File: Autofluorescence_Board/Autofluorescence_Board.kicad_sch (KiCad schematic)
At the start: 0 parts

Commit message: I have no idea
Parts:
- added U1: PAM2863ECR, SOIC_863ECR_DIO, symbol AF_SymbolLibrary:PAM2863ECR
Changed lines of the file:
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@@
 	(generator_version "10.0")
 	(paper "A4")
+	(symbol
+		(lib_id "AF_SymbolLibrary:PAM2863ECR")
+		(at 58.42 60.96 0)
+		(unit 1)
+		(body_style 1)
+		(exclude_from_sim no)
+		(in_bom yes)
+		(on_board yes)
+		(in_pos_files yes)
+		(dnp no)
+		(fields_autoplaced yes)
+		(property "Reference" "U1"
+			(at 81.28 50.8 0)
+			(show_name no)
+			(do_not_autoplace no)
+			(effects
+				(font
+					(size 1.524 1.524)
+				)
+			)
+		)
+		(property "Value" "PAM2863ECR"
+			(at 81.28 53.34 0)
+			(show_name no)
+			(do_not_autoplace no)
+			(effects
+				(font
+					(size 1.524 1.524)
+				)
+			)
+		)
+		(property "Footprint" "SOIC_863ECR_DIO"
+			(at 58.42 60.96 0)
+			(hide yes)
+			(show_name no)
+			(do_not_autoplace no)
+			(effects
+				(font
+					(size 1.27 1.27)
+					(italic yes)
+				)
+			)
+		)
+		(property "Datasheet" "PAM2863ECR"
+			(at 58.42 60.96 0)
+			(hide yes)
+			(show_name no)
+			(do_not_autoplace no)
+			(effects
+				(font
+					(size 1.27 1.27)
+					(italic yes)
+				)
+			)
+		)
+		(property "Description" ""
+			(at 58.42 60.96 0)
+			(hide yes)
+			(show_name no)
+			(do_not_autoplace no)
+			(effects
+				(font
+					(size 1.27 1.27)
+				)
+			)
+		)
+		(pin "1"
+		)
+		(pin "2"
+		)
+		(pin "5"
+		)
+		(pin "6"
+		)
+		(pin "4"
+		)
+		(pin "3"
+		)
+		(pin "8"
+		)
+		(pin "7"
+		)
+		(pin "EPAD"
+		)
+		(instances
+			(project "Autofluorescence_Board"
+				(path "/72deb9c7-3e3f-41e9-884c-65f2f5e1cc20"
+					(reference "U1")
+					(unit 1)
+				)
+			)
+		)
+	)
 	(sheet_instances
 		(path "/"

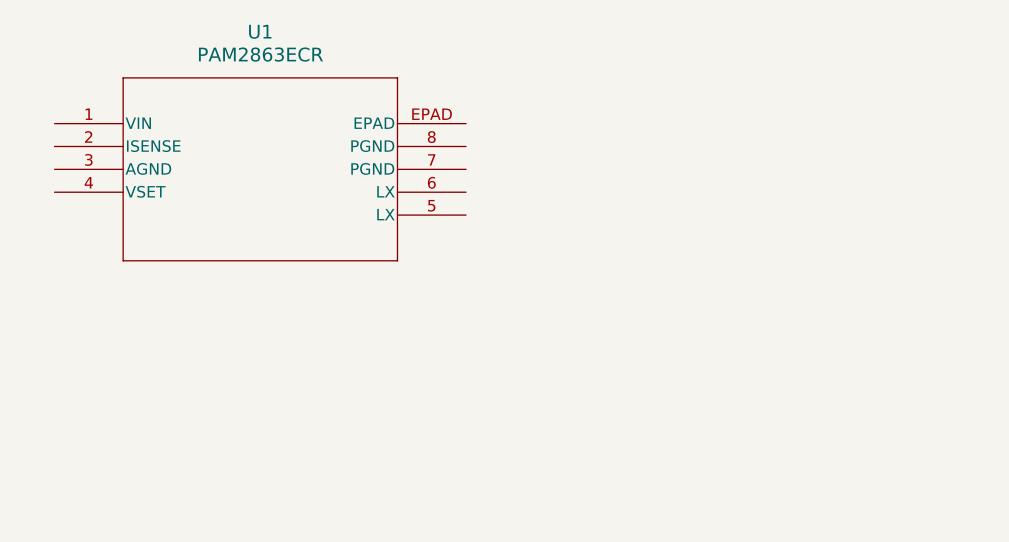
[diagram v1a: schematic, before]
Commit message: Added components to Schematic
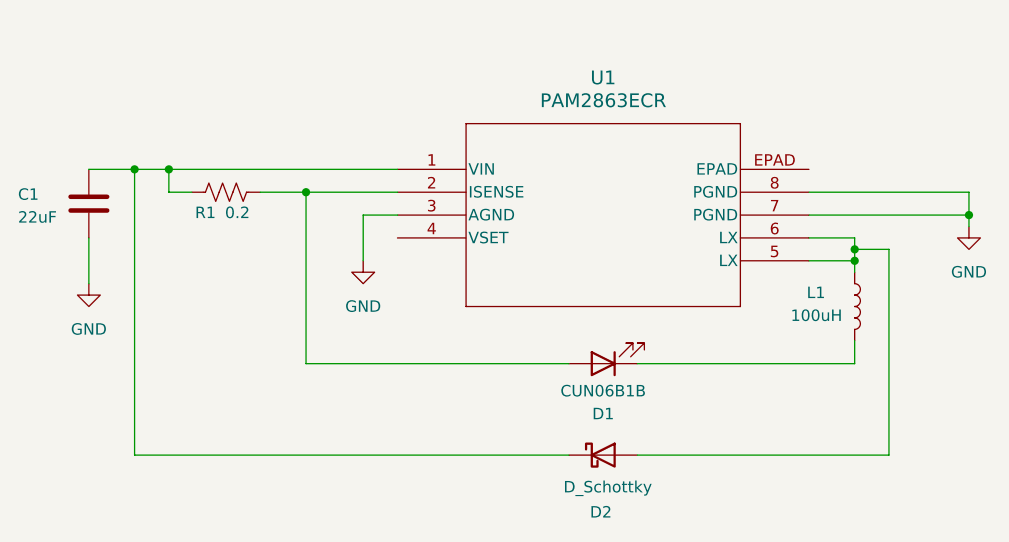
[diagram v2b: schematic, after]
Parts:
- added C1: 22uF, symbol Device:C
- added D1: CUN06B1B, symbol Device:LED
- added D2: D_Schottky, symbol Device:D_Schottky
- added L1: 100uH, symbol Device:L
- added R1: 0.2, symbol Device:R_US
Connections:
- net at U1.1 (VIN): now also C1.1, D2.1 (K), R1.1
- net at U1.2 (ISENSE): now also D1.2 (A), R1.2
- net GND: now reaches U1.3 (AGND)
- net GND: now also U1.7 (PGND), U1.8 (PGND), C1.2
- net at U1.5 (LX): now also U1.6 (LX), D2.2 (A), L1.1
- new net: D1.1 (K), L1.2
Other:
- moved on the sheet: U1

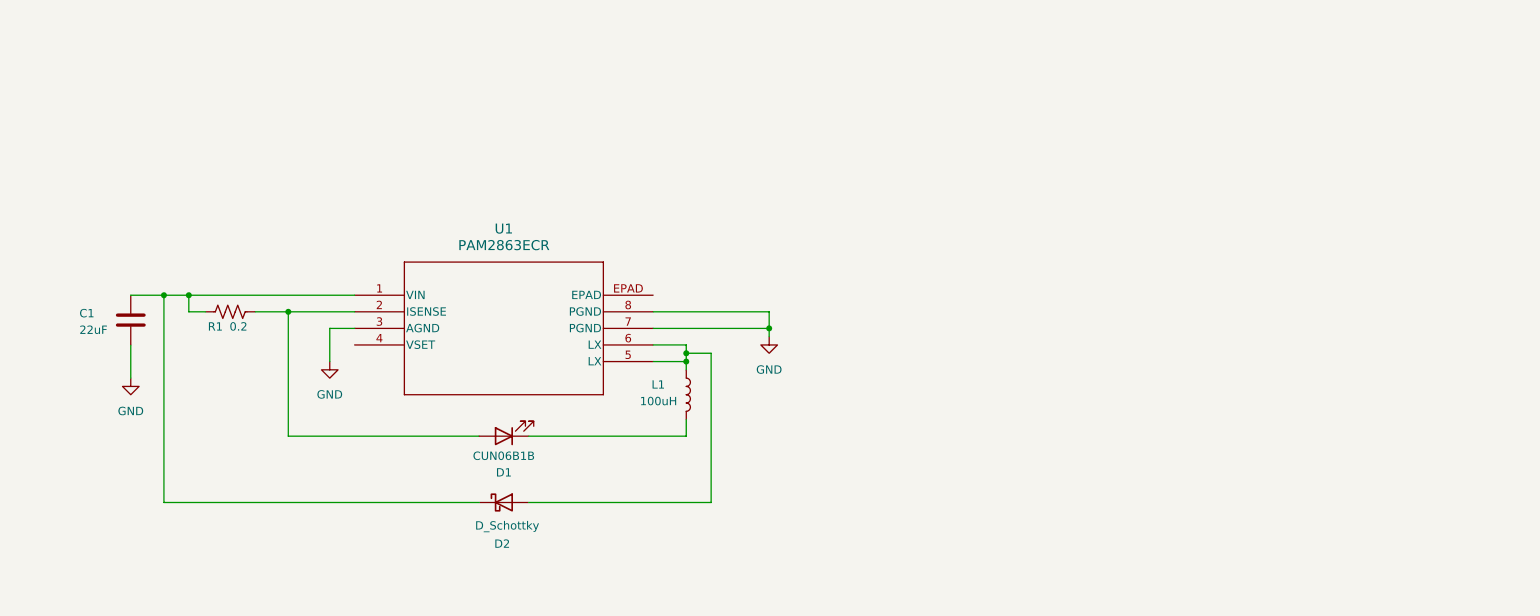
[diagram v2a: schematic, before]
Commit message: Added connectors and LEDs
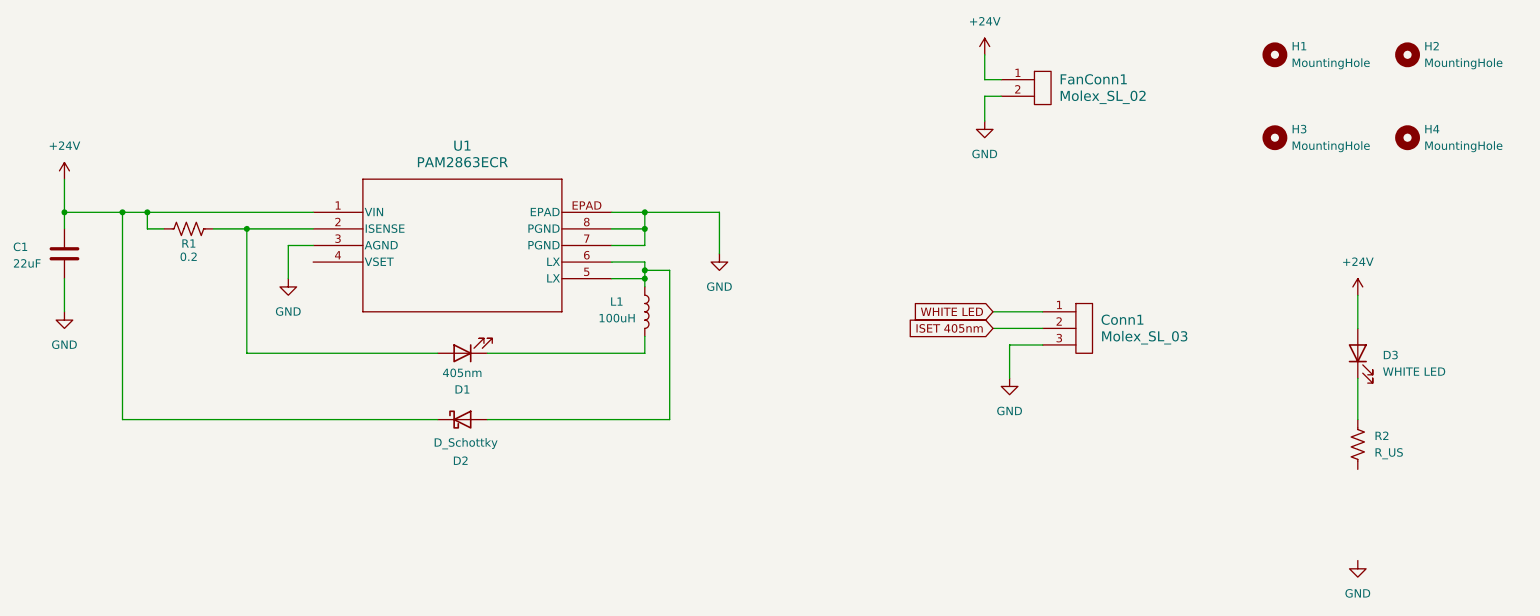
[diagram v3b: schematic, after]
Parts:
- added Conn1: Molex_SL_03, symbol MRDT_Connectors:Molex_SL_03
- added D3: WHITE LED, symbol Device:LED
- added FanConn1: Molex_SL_02, symbol MRDT_Connectors:Molex_SL_02
- added H1, H2, H3, H4: MountingHole, symbol Mechanical:MountingHole
- added R2: R_US, symbol Device:R_US
- D1: value CUN06B1B -> 405nm
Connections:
- net GND: now also U1.EPAD, Conn1.3, FanConn1.2
- net +24V: now reaches C1.1, D2.1 (K), R1.1, U1.1 (VIN)
- net +24V: now also D3.2 (A), FanConn1.1
- new net: D3.1 (K), R2.1
- new net ISET 405nm: Conn1.2
- new net WHITE LED: Conn1.1
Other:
- moved on the sheet: C1, D1, D2, L1, R1, U1

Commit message: Footprints Added, and all the other stuff -morgan
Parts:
- removed C1: 22uF, symbol Device:C
- removed Conn1: Molex_SL_03, symbol MRDT_Connectors:Molex_SL_03
- removed D1: 405nm, symbol Device:LED
- removed D2: D_Schottky, symbol Device:D_Schottky
- removed FanConn1: Molex_SL_02, symbol MRDT_Connectors:Molex_SL_02
- removed L1: 100uH, symbol Device:L
- removed R1: 0.2, symbol Device:R_US
- removed U1: PAM2863ECR, SOIC_863ECR_DIO, symbol AF_SymbolLibrary:PAM2863ECR
- added C2: 22uF, Capacitor_SMD:C_0603_1608Metric_Pad1.08x0.95mm_HandSolder, symbol Device:C
- added D4: D_Schottky, Diode_SMD:D_SOD-123, symbol Device:D_Schottky
- added D6: 10V, Package_DIP:DIP-40_W15.24mm, symbol Device:D_Zener
- added H5, H6, H7, H8: MountingHole_Pad, Package_DFN_QFN:Nordic_AQFN-94-1EP_7x7mm_P0.4mm, symbol Mechanical:MountingHole_Pad
- added J1: Conn_01x04, Package_DFN_QFN:QFN-20-1EP_5x5mm_P0.65mm_EP3.35x3.35mm, symbol Connector_Generic:Conn_01x04
- added J2, J3, J5: Conn_01x02, Package_DFN_QFN:QFN-20-1EP_5x5mm_P0.65mm_EP3.35x3.35mm, symbol Connector_Generic:Conn_01x02
- added J4: Conn_01x04, symbol Connector_Generic:Conn_01x04
- added L2: 100uH, Inductor_SMD:L_0201_0603Metric_Pad0.64x0.40mm_HandSolder, symbol Device:L
- added Q1: A03401A, Package_TO_SOT_SMD:SOT-23, symbol Device:Q_PMOS
- added Q2: BSS138, Package_TO_SOT_SMD:SOT-23, symbol Transistor_FET:BSS138
- added R3: 0.2, Resistor_SMD:R_0603_1608Metric_Pad0.98x0.95mm_HandSolder, symbol Device:R_US
- added R4: 10K, Resistor_SMD:R_0603_1608Metric_Pad0.98x0.95mm_HandSolder, symbol Device:R_US
- added U2: PAM2863ECR, Package_SO:Diodes_SO-8EP, symbol AF_SymbolLibrary:PAM2863ECR
- D3: footprint (none) -> Diode_SMD:D_0603_1608Metric_Pad1.05x0.95mm_HandSolder
- R2: value R_US -> 5K; footprint (none) -> Resistor_SMD:R_0603_1608Metric_Pad0.98x0.95mm_HandSolder
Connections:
- net GND: now also C2.2, H5.1, H6.1, H7.1, H8.1, J1.4 (Pin_4), J2.2 (Pin_2), J4.4 (Pin_4), J5.2 (Pin_2), Q2.2 (S), R4.2, U2.3 (AGND), U2.7 (PGND), U2.8 (PGND), U2.EPAD
- net ISET 405nm: now also J4.2 (Pin_2)
- net WHITE LED: now also J4.1 (Pin_1), Q2.1 (G)
- net at R2.2: now also Q2.3 (D)
- net +24V renamed Vbat
- net Vbat: now also J5.1 (Pin_1), Q1.S
- new net: C2.1, D4.1 (K), R3.1, U2.1 (VIN)
- new net: J3.2 (Pin_2), R3.2, U2.2 (ISENSE)
- new net: D4.2 (A), L2.1, U2.5 (LX), U2.6 (LX)
- new net: D6.2 (A), Q1.G, R4.1
- new net: J3.1 (Pin_1), L2.2
- new net PWM: U2.4 (VSET)
- new net UV LED PWM: J1.1 (Pin_1)
- new net Vfan: J2.1 (Pin_1)
- new net Vin: D6.1 (K), J4.3 (Pin_3), Q1.D
- new net White LED PWM: J1.2 (Pin_2)
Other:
- moved on the sheet: D3, R2

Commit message: lets try this gain again
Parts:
- removed H5, H6, H7, H8: MountingHole_Pad, Package_DFN_QFN:Nordic_AQFN-94-1EP_7x7mm_P0.4mm, symbol Mechanical:MountingHole_Pad

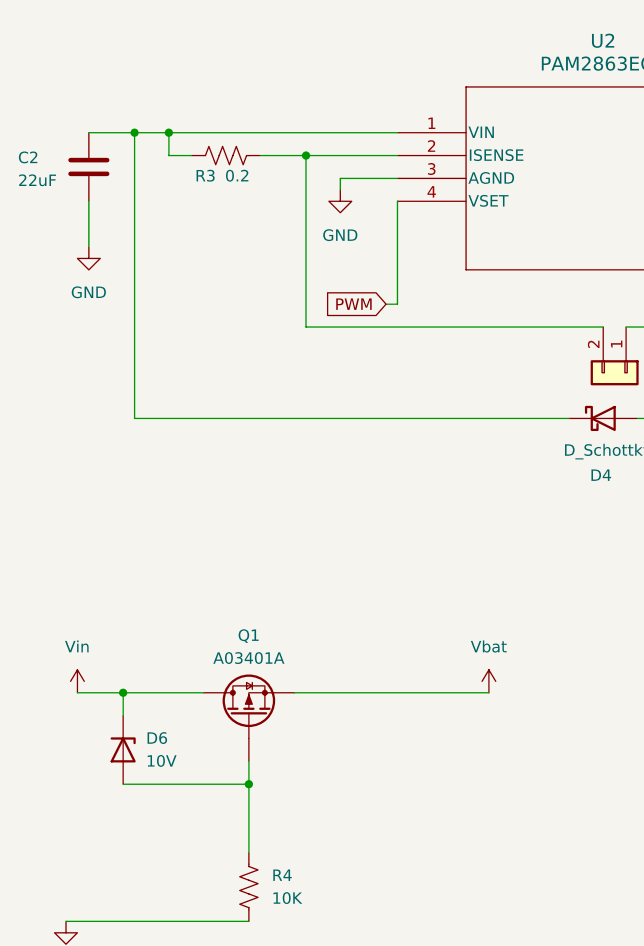
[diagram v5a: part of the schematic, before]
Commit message: Fixed nets and a couple of values
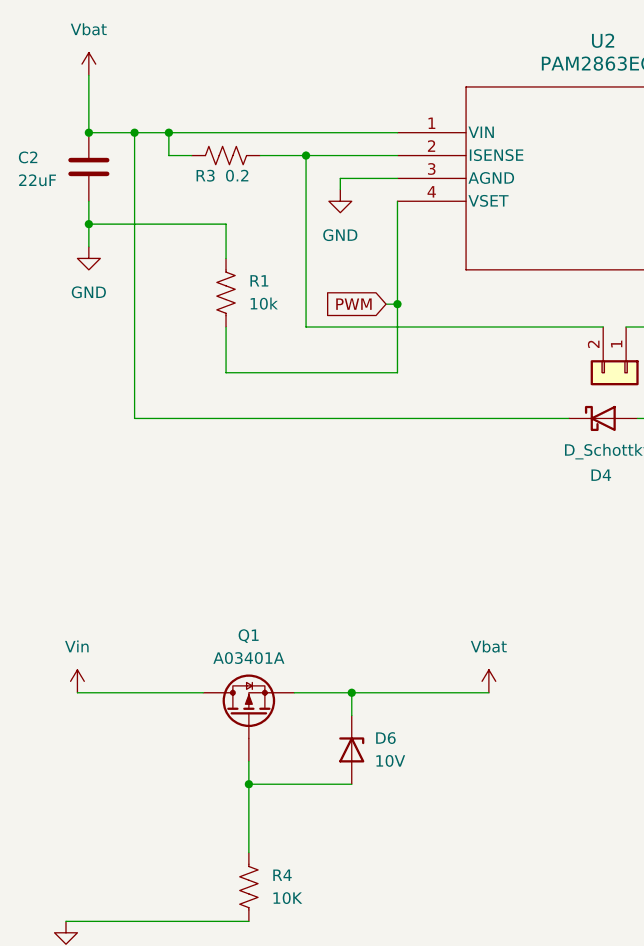
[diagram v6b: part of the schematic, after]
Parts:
- added R1: 10k, Package_DIP:DIP-8_W7.62mm, symbol Device:R_US
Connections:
- net GND: now also R1.2
- net PWM: now also R1.1
- net Vbat: now also C2.1, D4.1 (K), D6.1 (K), R3.1, U2.1 (VIN)
- net Vin: no longer D6.1 (K)
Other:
- moved on the sheet: D6

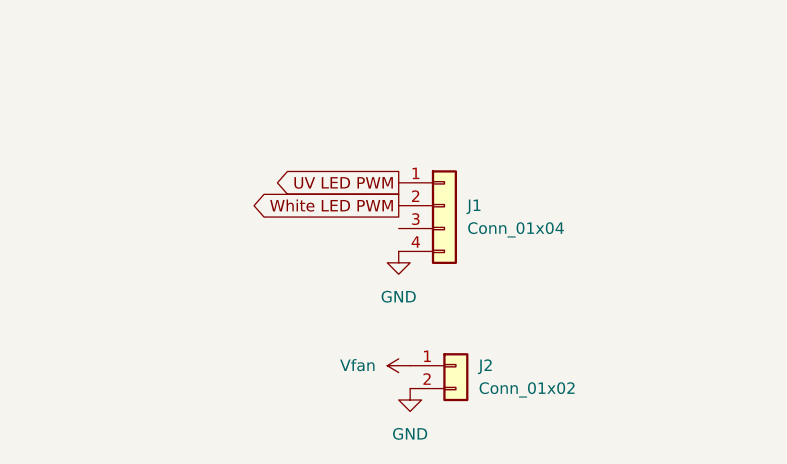
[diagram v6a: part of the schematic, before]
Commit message: Small values fixes, and net additions
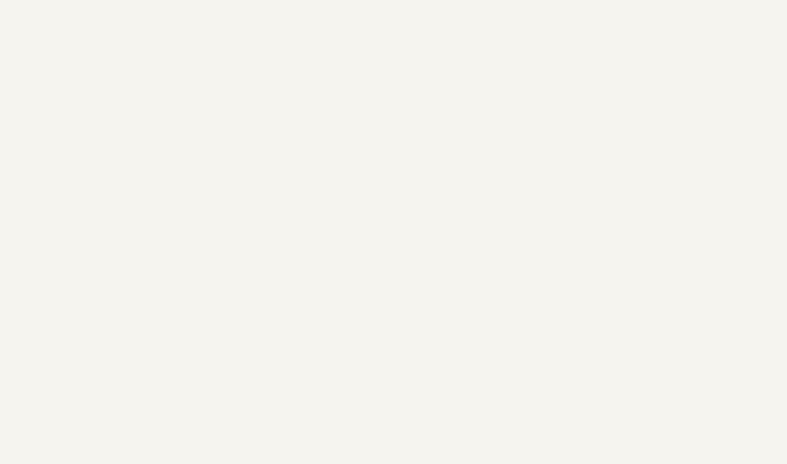
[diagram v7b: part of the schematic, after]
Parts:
- removed J1: Conn_01x04, Package_DFN_QFN:QFN-20-1EP_5x5mm_P0.65mm_EP3.35x3.35mm, symbol Connector_Generic:Conn_01x04
- removed J2: Conn_01x02, Package_DFN_QFN:QFN-20-1EP_5x5mm_P0.65mm_EP3.35x3.35mm, symbol Connector_Generic:Conn_01x02

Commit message: Added JST Footprints
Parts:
- J3, J5: footprint Package_DFN_QFN:QFN-20-1EP_5x5mm_P0.65mm_EP3.35x3.35mm -> Connector_JST:JST_PH_B2B-PH-K_1x02_P2.00mm_Vertical
- J4: footprint (none) -> Connector_JST:JST_PH_B4B-PH-K_1x04_P2.00mm_Vertical
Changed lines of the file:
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@@
 			)
 		)
-		(property "Footprint" "Package_DFN_QFN:QFN-20-1EP_5x5mm_P0.65mm_EP3.35x3.35mm"
+		(property "Footprint" "Connector_JST:JST_PH_B2B-PH-K_1x02_P2.00mm_Vertical"
 			(at 90.17 58.42 0)
 			(hide yes)
@@
 			)
 		)
-		(property "Footprint" "Package_DFN_QFN:QFN-20-1EP_5x5mm_P0.65mm_EP3.35x3.35mm"
+		(property "Footprint" "Connector_JST:JST_PH_B2B-PH-K_1x02_P2.00mm_Vertical"
 			(at 200.66 33.02 0)
 			(hide yes)
@@
 			)
 		)
-		(property "Footprint" ""
+		(property "Footprint" "Connector_JST:JST_PH_B4B-PH-K_1x04_P2.00mm_Vertical"
 			(at 171.45 58.42 0)
 			(hide yes)
